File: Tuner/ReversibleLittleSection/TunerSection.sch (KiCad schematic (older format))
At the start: 113 parts, among them J1 Conn_01x03, J10 Conn_01x02, J11 Conn_02x05_Odd_Even, J12 Conn_01x01, J13 Conn_01x01, J14 Conn_01x01, J15 Conn_01x01, J2 Conn_01x03, J3 Conn_01x03, J4 Conn_01x03, J5 Conn_01x03, J6 Conn_01x03, J7 Conn_01x03, J8 Conn_01x02, J9 Conn_01x02, P10 Conn_01x01, P11 Conn_01x01, P12 Conn_01x01, P2 Conn_01x01, P3 Conn_01x01, P4 Conn_01x01, P5 Conn_01x01, P6 Conn_01x01, P7 Conn_01x01, P8 Conn_01x01, P9 Conn_01x01, U1 MCP23008, U2 ULN2803A

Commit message: JLCPCB Nov 1 2018
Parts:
- removed C36, C37: 10 nF, Capacitors_THT:C_Disc_D5.0mm_W2.5mm_P5.00mm, symbol C
- added J16, J17, J18, J19, J20, J21, J22: Conn_01x01, tuner:SOLDERJUMPER, symbol Conn_01x01
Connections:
- net RFGND: now also J16.1 (Pin_1)
- net at J9.2 (Pin_2), RLY9.2 (NC): now also J22.1 (Pin_1)
- net at J10.2 (Pin_2), RLY9.3 (NO): now also J17.1 (Pin_1)
- net at J15.1 (Pin_1): now also J18.1 (Pin_1), J19.1 (Pin_1)
- net at J12.1 (Pin_1): now also J20.1 (Pin_1), J21.1 (Pin_1)
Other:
- moved on the sheet: J15
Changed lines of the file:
@@
 RLY8
 $Comp
-L +5V #PWR13
+L +5V #PWR01
 U 1 1 5B1A0287
 P 3150 5750
-F 0 "#PWR13" H 3150 5600 50  0001 C CNN
+F 0 "#PWR01" H 3150 5600 50  0001 C CNN
 F 1 "+5V" H 3150 5890 50  0000 C CNN
 F 2 "" H 3150 5750 50  0001 C CNN
@@
 $EndComp
 $Comp
-L GND #PWR3
+L GND #PWR02
 U 1 1 5B1AA0F6
 P 900 4500
-F 0 "#PWR3" H 900 4250 50  0001 C CNN
+F 0 "#PWR02" H 900 4250 50  0001 C CNN
 F 1 "GND" H 900 4350 50  0000 C CNN
 F 2 "" H 900 4500 50  0001 C CNN
@@
 $EndComp
 $Comp
-L +5V #PWR2
+L +5V #PWR03
 U 1 1 5B1AABE9
 P 900 3750
-F 0 "#PWR2" H 900 3600 50  0001 C CNN
+F 0 "#PWR03" H 900 3600 50  0001 C CNN
 F 1 "+5V" H 900 3890 50  0000 C CNN
 F 2 "" H 900 3750 50  0001 C CNN
@@
 $EndComp
 $Comp
-L +5V #PWR9
+L +5V #PWR04
 U 1 1 5B1ABA5A
 P 2150 4450
-F 0 "#PWR9" H 2150 4300 50  0001 C CNN
+F 0 "#PWR04" H 2150 4300 50  0001 C CNN
 F 1 "+5V" H 2150 4590 50  0000 C CNN
 F 2 "" H 2150 4450 50  0001 C CNN
@@
 $EndComp
 $Comp
-L +5V #PWR11
+L +5V #PWR05
 U 1 1 5B1ABCDE
 P 2400 3950
-F 0 "#PWR11" H 2400 3800 50  0001 C CNN
+F 0 "#PWR05" H 2400 3800 50  0001 C CNN
 F 1 "+5V" H 2400 4090 50  0000 C CNN
 F 2 "" H 2400 3950 50  0001 C CNN
@@
 $EndComp
 $Comp
-L +5V #PWR17
+L +5V #PWR06
 U 1 1 5B1ABFC6
 P 8800 4600
-F 0 "#PWR17" H 8800 4450 50  0001 C CNN
+F 0 "#PWR06" H 8800 4450 50  0001 C CNN
 F 1 "+5V" H 8800 4740 50  0000 C CNN
 F 2 "" H 8800 4600 50  0001 C CNN
@@
 $EndComp
 $Comp
-L GND #PWR18
+L GND #PWR07
 U 1 1 5B1AC04C
 P 8800 5050
-F 0 "#PWR18" H 8800 4800 50  0001 C CNN
+F 0 "#PWR07" H 8800 4800 50  0001 C CNN
 F 1 "GND" H 8800 4900 50  0000 C CNN
 F 2 "" H 8800 5050 50  0001 C CNN
@@
 L Conn_01x01 J15
 U 1 1 5B19812D
-P 10950 950
-F 0 "J15" H 10950 1050 50  0000 C CNN
-F 1 "Conn_01x01" H 10950 850 50  0000 C CNN
-F 2 "Connectors:1pin" H 10950 950 50  0001 C CNN
-F 3 "" H 10950 950 50  0001 C CNN
-	1    10950 950
-	1    0    0    -1
-$EndComp
-$Comp
-L Conn_01x01 J12
-U 1 1 5B1981D8
-P 10950 1250
-F 0 "J12" H 10950 1350 50  0000 C CNN
-F 1 "Conn_01x01" H 10950 1150 50  0000 C CNN
-F 2 "Connectors:1pin" H 10950 1250 50  0001 C CNN
-F 3 "" H 10950 1250 50  0001 C CNN
-	1    10950 1250
+P 11100 750
+F 0 "J15" H 11100 850 50  0000 C CNN
+F 1 "Conn_01x01" H 11100 650 50  0000 C CNN
+F 2 "Connectors:1pin" H 11100 750 50  0001 C CNN
+F 3 "" H 11100 750 50  0001 C CNN
+	1    11100 750
 	1    0    0    -1
 $EndComp
@@
 $EndComp
 $Comp
-L +5V #PWR10
+L +5V #PWR08
 U 1 1 5B196BCE
 P 2250 3950
-F 0 "#PWR10" H 2250 3800 50  0001 C CNN
+F 0 "#PWR08" H 2250 3800 50  0001 C CNN
 F 1 "+5V" H 2250 4090 50  0000 C CNN
 F 2 "" H 2250 3950 50  0001 C CNN
@@
 $EndComp
 $Comp
-L GND #PWR15
+L GND #PWR09
 U 1 1 5B9A4AE1
 P 4850 6650
-F 0 "#PWR15" H 4850 6400 50  0001 C CNN
+F 0 "#PWR09" H 4850 6400 50  0001 C CNN
 F 1 "GND" H 4850 6500 50  0000 C CNN
 F 2 "" H 4850 6650 50  0001 C CNN
@@
 $EndComp
 $Comp
-L GND #PWR12
+L GND #PWR010
 U 1 1 5B9A6036
 P 3150 4200
-F 0 "#PWR12" H 3150 3950 50  0001 C CNN
+F 0 "#PWR010" H 3150 3950 50  0001 C CNN
 F 1 "GND" H 3150 4050 50  0000 C CNN
 F 2 "" H 3150 4200 50  0001 C CNN
@@
 $EndComp
 $Comp
-L GND #PWR14
+L GND #PWR011
 U 1 1 5B9ACA36
 P 3550 6100
-F 0 "#PWR14" H 3550 5850 50  0001 C CNN
+F 0 "#PWR011" H 3550 5850 50  0001 C CNN
 F 1 "GND" H 3550 5950 50  0000 C CNN
 F 2 "" H 3550 6100 50  0001 C CNN
@@
 $EndComp
 $Comp
-L GND #PWR19
+L GND #PWR012
 U 1 1 5B982525
 P 9850 2000
-F 0 "#PWR19" H 9850 1750 50  0001 C CNN
+F 0 "#PWR012" H 9850 1750 50  0001 C CNN
 F 1 "GND" H 9850 1850 50  0000 C CNN
 F 2 "" H 9850 2000 50  0001 C CNN
@@
 $EndComp
 $Comp
-L GND #PWR7
+L GND #PWR013
 U 1 1 5BA4D8F3
 P 1800 5850
-F 0 "#PWR7" H 1800 5600 50  0001 C CNN
+F 0 "#PWR013" H 1800 5600 50  0001 C CNN
 F 1 "GND" H 1800 5700 50  0000 C CNN
 F 2 "" H 1800 5850 50  0001 C CNN
@@
 $EndComp
 $Comp
-L +5V #PWR8
+L +5V #PWR014
 U 1 1 5BA4E273
 P 1850 5300
-F 0 "#PWR8" H 1850 5150 50  0001 C CNN
+F 0 "#PWR014" H 1850 5150 50  0001 C CNN
 F 1 "+5V" H 1850 5440 50  0000 C CNN
 F 2 "" H 1850 5300 50  0001 C CNN
@@
 $EndComp
 $Comp
-L +5V #PWR6
+L +5V #PWR015
 U 1 1 5BA4E663
 P 1200 5700
-F 0 "#PWR6" H 1200 5550 50  0001 C CNN
+F 0 "#PWR015" H 1200 5550 50  0001 C CNN
 F 1 "+5V" H 1200 5840 50  0000 C CNN
 F 2 "" H 1200 5700 50  0001 C CNN
@@
 $EndComp
 $Comp
-L GND #PWR1
+L GND #PWR016
 U 1 1 5BA4FB25
 P 750 5900
-F 0 "#PWR1" H 750 5650 50  0001 C CNN
+F 0 "#PWR016" H 750 5650 50  0001 C CNN
 F 1 "GND" H 750 5750 50  0000 C CNN
 F 2 "" H 750 5900 50  0001 C CNN
@@
 $EndComp
 $Comp
-L GND #PWR5
+L GND #PWR017
 U 1 1 5BA5005D
 P 1100 5300
-F 0 "#PWR5" H 1100 5050 50  0001 C CNN
+F 0 "#PWR017" H 1100 5050 50  0001 C CNN
 F 1 "GND" H 1100 5150 50  0000 C CNN
 F 2 "" H 1100 5300 50  0001 C CNN
@@
 EXTPWR
 $Comp
-L +5V #PWR4
+L +5V #PWR018
 U 1 1 5BAE4DBC
 P 1000 4850
-F 0 "#PWR4" H 1000 4700 50  0001 C CNN
+F 0 "#PWR018" H 1000 4700 50  0001 C CNN
 F 1 "+5V" H 1000 4990 50  0000 C CNN
 F 2 "" H 1000 4850 50  0001 C CNN
@@
 	700  4850 1000 4850
 $Comp
-L GND #PWR16
+L GND #PWR019
 U 1 1 5BAEE216
 P 5050 7250
-F 0 "#PWR16" H 5050 7000 50  0001 C CNN
+F 0 "#PWR019" H 5050 7000 50  0001 C CNN
 F 1 "GND" H 5050 7100 50  0000 C CNN
 F 2 "" H 5050 7250 50  0001 C CNN
@@
 	10400 2550 10400 2250
 Connection ~ 10400 2250
-Text GLabel 10100 1250 0    60   Input ~ 0
+Text GLabel 9550 750  0    60   Input ~ 0
 RFGND
 $Comp
-L C C37
-U 1 1 5BCC2C84
-P 10500 1250
-F 0 "C37" H 10525 1350 50  0000 L CNN
-F 1 "10 nF" H 10525 1150 50  0000 L CNN
-F 2 "Capacitors_THT:C_Disc_D5.0mm_W2.5mm_P5.00mm" H 10538 1100 50  0001 C CNN
-F 3 "" H 10500 1250 50  0001 C CNN
-	1    10500 1250
-	0    1    1    0
-$EndComp
-Wire Wire Line
-	10650 1250 10750 1250
-Wire Wire Line
-	10100 1250 10350 1250
-$Comp
-L C C36
-U 1 1 5BCFB23A
-P 10500 950
-F 0 "C36" H 10525 1050 50  0000 L CNN
-F 1 "10 nF" H 10525 850 50  0000 L CNN
-F 2 "Capacitors_THT:C_Disc_D5.0mm_W2.5mm_P5.00mm" H 10538 800 50  0001 C CNN
-F 3 "" H 10500 950 50  0001 C CNN
-	1    10500 950
-	0    1    1    0
-$EndComp
-Text GLabel 10100 950  0    60   Input ~ 0
-RFGND
-Wire Wire Line
-	10100 950  10350 950
-Wire Wire Line
-	10650 950  10750 950
+L Conn_01x01 J16
+U 1 1 5BD88254
+P 9850 750
+F 0 "J16" H 9850 850 50  0000 C CNN
+F 1 "Conn_01x01" H 9850 650 50  0000 C CNN
+F 2 "tuner:SOLDERJUMPER" H 9850 750 50  0001 C CNN
+F 3 "" H 9850 750 50  0001 C CNN
+	1    9850 750
+	1    0    0    -1
+$EndComp
+Wire Wire Line
+	9650 750  9550 750
+$Comp
+L Conn_01x01 J18
+U 1 1 5BD8893E
+P 10650 700
+F 0 "J18" H 10650 800 50  0000 C CNN
+F 1 "Conn_01x01" H 10650 600 50  0000 C CNN
+F 2 "tuner:SOLDERJUMPER" H 10650 700 50  0001 C CNN
+F 3 "" H 10650 700 50  0001 C CNN
+	1    10650 700
+	-1   0    0    1
+$EndComp
+$Comp
+L Conn_01x01 J19
+U 1 1 5BD88AB6
+P 10650 800
+F 0 "J19" H 10650 900 50  0000 C CNN
+F 1 "Conn_01x01" H 10650 700 50  0000 C CNN
+F 2 "tuner:SOLDERJUMPER" H 10650 800 50  0001 C CNN
+F 3 "" H 10650 800 50  0001 C CNN
+	1    10650 800
+	-1   0    0    1
+$EndComp
+Wire Wire Line
+	10850 700  10850 800
+Wire Wire Line
+	10850 750  10900 750
+Connection ~ 10850 750
+$Comp
+L Conn_01x01 J22
+U 1 1 5BD890B9
+P 9600 3750
+F 0 "J22" H 9600 3850 50  0000 C CNN
+F 1 "Conn_01x01" H 9600 3650 50  0000 C CNN
+F 2 "tuner:SOLDERJUMPER" H 9600 3750 50  0001 C CNN
+F 3 "" H 9600 3750 50  0001 C CNN
+	1    9600 3750
+	-1   0    0    1
+$EndComp
+$Comp
+L Conn_01x01 J20
+U 1 1 5BD8922D
+P 10650 950
+F 0 "J20" H 10650 1050 50  0000 C CNN
+F 1 "Conn_01x01" H 10650 850 50  0000 C CNN
+F 2 "tuner:SOLDERJUMPER" H 10650 950 50  0001 C CNN
+F 3 "" H 10650 950 50  0001 C CNN
+	1    10650 950
+	-1   0    0    1
+$EndComp
+$Comp
+L Conn_01x01 J21
+U 1 1 5BD8939E
+P 10650 1050
+F 0 "J21" H 10650 1150 50  0000 C CNN
+F 1 "Conn_01x01" H 10650 950 50  0000 C CNN
+F 2 "tuner:SOLDERJUMPER" H 10650 1050 50  0001 C CNN
+F 3 "" H 10650 1050 50  0001 C CNN
+	1    10650 1050
+	-1   0    0    1
+$EndComp
+Wire Wire Line
+	10850 950  10850 1050
+Wire Wire Line
+	10850 1000 10900 1000
+Connection ~ 10850 1000
+$Comp
+L Conn_01x01 J17
+U 1 1 5BD89B92
+P 10500 4000
+F 0 "J17" H 10500 4100 50  0000 C CNN
+F 1 "Conn_01x01" H 10500 3900 50  0000 C CNN
+F 2 "tuner:SOLDERJUMPER" H 10500 4000 50  0001 C CNN
+F 3 "" H 10500 4000 50  0001 C CNN
+	1    10500 4000
+	1    0    0    -1
+$EndComp
+Wire Wire Line
+	10300 4000 10150 4000
+Connection ~ 10150 4000
+$Comp
+L Conn_01x01 J12
+U 1 1 5BD8A2D9
+P 11100 1000
+F 0 "J12" H 11100 1100 50  0000 C CNN
+F 1 "Conn_01x01" H 11100 900 50  0000 C CNN
+F 2 "Connectors:1pin" H 11100 1000 50  0001 C CNN
+F 3 "" H 11100 1000 50  0001 C CNN
+	1    11100 1000
+	1    0    0    -1
+$EndComp
+Wire Wire Line
+	9800 3750 9900 3750
+Connection ~ 9900 3750
 $EndSCHEMATC

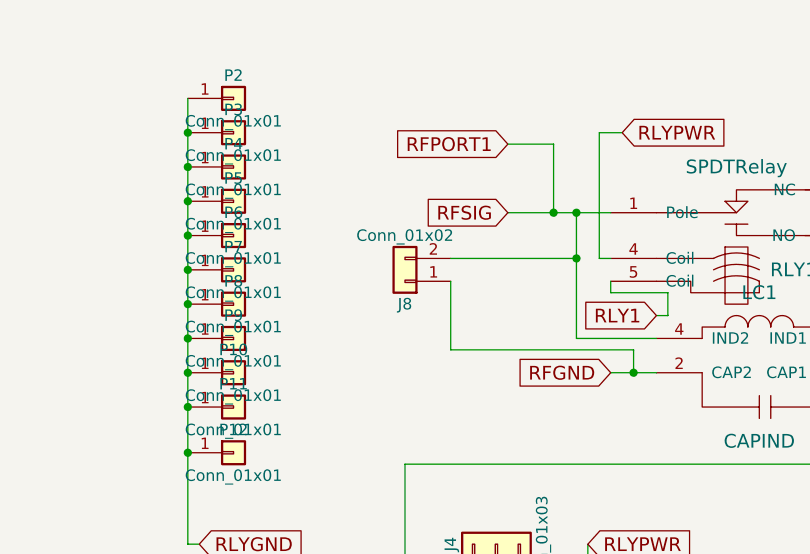
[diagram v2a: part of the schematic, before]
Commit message: Modified connectors on Reversible boards
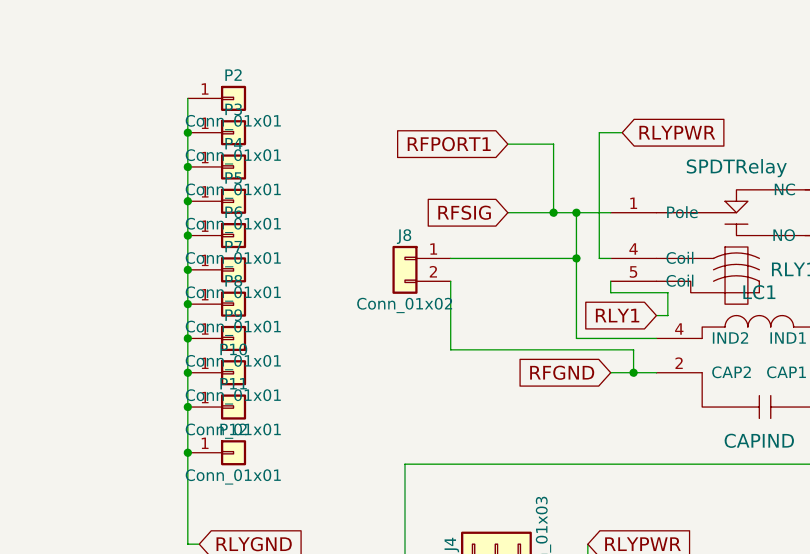
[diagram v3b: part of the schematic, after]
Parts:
- J10, J8, J9: footprint Connectors_Terminal_Blocks:TerminalBlock_bornier-2_P5.08mm -> tuner:bnc_90_1-1337543-0_pad_combo
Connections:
- net RFGND: now also J8.2 (Pin_2); no longer J8.1 (Pin_1)
- net RFPORT1: now also J8.1 (Pin_1); no longer J8.2 (Pin_2)
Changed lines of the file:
@@
 L Conn_01x02 J8
 U 1 1 5B18E79B
-P 2150 1700
-F 0 "J8" H 2150 1800 50  0000 C CNN
-F 1 "Conn_01x02" H 2150 1500 50  0000 C CNN
-F 2 "Connectors_Terminal_Blocks:TerminalBlock_bornier-2_P5.08mm" H 2150 1700 50  0001 C CNN
-F 3 "" H 2150 1700 50  0001 C CNN
-	1    2150 1700
-	-1   0    0    1
+P 2150 1600
+F 0 "J8" H 2150 1700 50  0000 C CNN
+F 1 "Conn_01x02" H 2150 1400 50  0000 C CNN
+F 2 "tuner:bnc_90_1-1337543-0_pad_combo" H 2150 1600 50  0001 C CNN
+F 3 "" H 2150 1600 50  0001 C CNN
+	1    2150 1600
+	-1   0    0    -1
 $EndComp
 $Comp
@@
 F 0 "J10" H 10350 3700 50  0000 C CNN
 F 1 "Conn_01x02" H 10350 3400 50  0000 C CNN
-F 2 "Connectors_Terminal_Blocks:TerminalBlock_bornier-2_P5.08mm" H 10350 3600 50  0001 C CNN
+F 2 "tuner:bnc_90_1-1337543-0_pad_combo" H 10350 3600 50  0001 C CNN
 F 3 "" H 10350 3600 50  0001 C CNN
 	1    10350 3600
@@
 F 0 "J9" H 10350 3200 50  0000 C CNN
 F 1 "Conn_01x02" H 10350 2900 50  0000 C CNN
-F 2 "Connectors_Terminal_Blocks:TerminalBlock_bornier-2_P5.08mm" H 10350 3100 50  0001 C CNN
+F 2 "tuner:bnc_90_1-1337543-0_pad_combo" H 10350 3100 50  0001 C CNN
 F 3 "" H 10350 3100 50  0001 C CNN
 	1    10350 3100

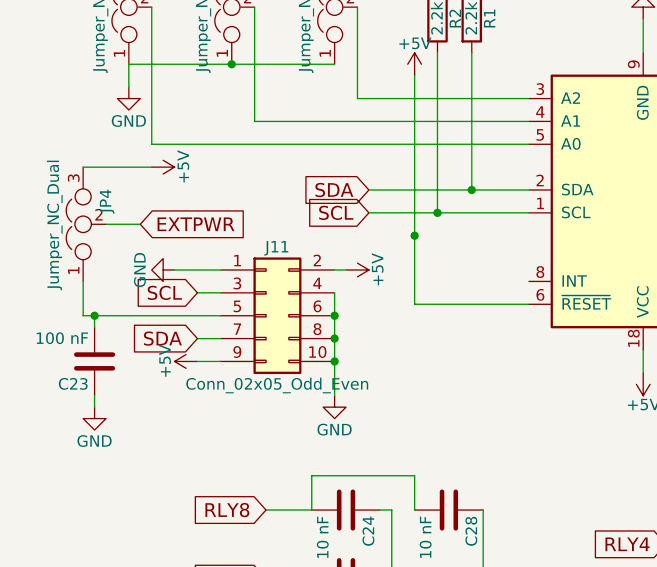
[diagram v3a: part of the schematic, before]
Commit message: Changed I2C cable pinoutgit add Tunergit add Tuner Also added ICOM rig support
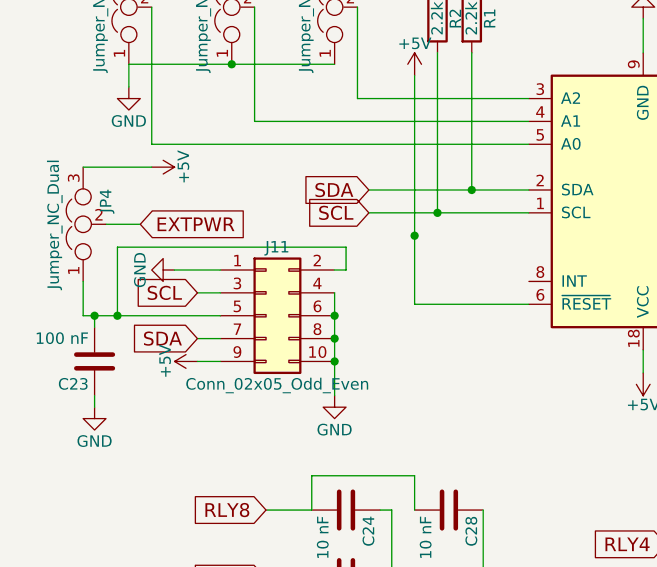
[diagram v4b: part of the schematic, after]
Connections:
- net +5V: no longer J11.2 (Pin_2)
- net at C23.2, J11.5 (Pin_5), JP4.1: now also J11.2 (Pin_2)
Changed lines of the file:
@@
-$EndComp
-$Comp
-L +5V #PWR8
-U 1 1 5BA4E273
-P 1850 5300
-F 0 "#PWR8" H 1850 5150 50  0001 C CNN
-F 1 "+5V" H 1850 5440 50  0000 C CNN
-F 2 "" H 1850 5300 50  0001 C CNN
-F 3 "" H 1850 5300 50  0001 C CNN
-	1    1850 5300
-	0    1    1    0
 $EndComp
 $Comp
@@
 	9800 3750 9900 3750
 Connection ~ 9900 3750
+Wire Wire Line
+	850  5500 850  5200
+Wire Wire Line
+	850  5200 1850 5200
+Wire Wire Line
+	1850 5200 1850 5300
+Connection ~ 850  5500
 $EndSCHEMATC

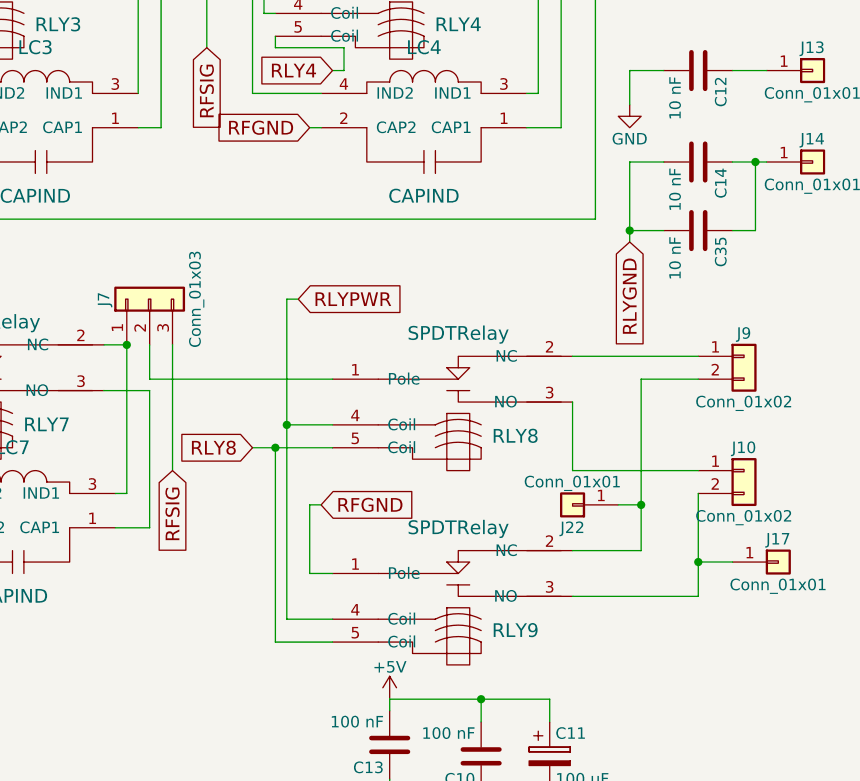
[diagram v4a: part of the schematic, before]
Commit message: Added nonswitched output to ReversibleSections
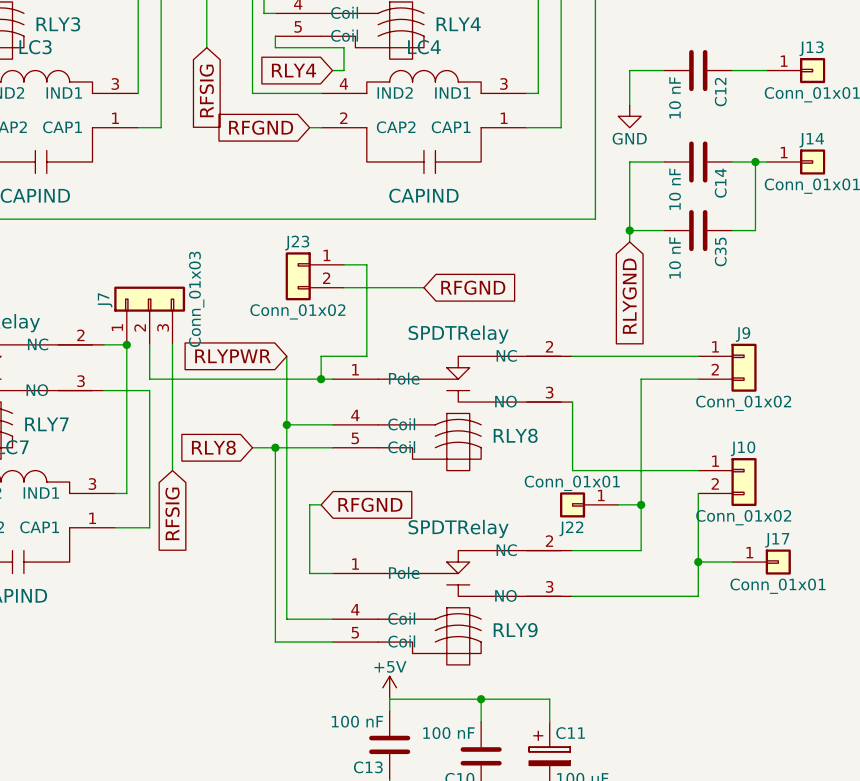
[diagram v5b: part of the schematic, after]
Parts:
- added J23: Conn_01x02, tuner:bnc_90_1-1337543-0_pad_combo, symbol Conn_01x02
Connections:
- net RFGND: now also J23.2 (Pin_2)
- net at J7.2 (Pin_2), RLY8.1 (Pole): now also J23.1 (Pin_1)
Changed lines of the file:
@@
 RLY8
 $Comp
-L +5V #PWR13
+L +5V #PWR12
 U 1 1 5B1A0287
 P 3150 5750
-F 0 "#PWR13" H 3150 5600 50  0001 C CNN
+F 0 "#PWR12" H 3150 5600 50  0001 C CNN
 F 1 "+5V" H 3150 5890 50  0000 C CNN
 F 2 "" H 3150 5750 50  0001 C CNN
@@
 $EndComp
 $Comp
-L +5V #PWR9
+L +5V #PWR8
 U 1 1 5B1ABA5A
 P 2150 4450
-F 0 "#PWR9" H 2150 4300 50  0001 C CNN
+F 0 "#PWR8" H 2150 4300 50  0001 C CNN
 F 1 "+5V" H 2150 4590 50  0000 C CNN
 F 2 "" H 2150 4450 50  0001 C CNN
@@
 $EndComp
 $Comp
-L +5V #PWR11
+L +5V #PWR10
 U 1 1 5B1ABCDE
 P 2400 3950
-F 0 "#PWR11" H 2400 3800 50  0001 C CNN
+F 0 "#PWR10" H 2400 3800 50  0001 C CNN
 F 1 "+5V" H 2400 4090 50  0000 C CNN
 F 2 "" H 2400 3950 50  0001 C CNN
@@
 $EndComp
 $Comp
-L +5V #PWR10
+L +5V #PWR9
 U 1 1 5B196BCE
 P 2250 3950
-F 0 "#PWR10" H 2250 3800 50  0001 C CNN
+F 0 "#PWR9" H 2250 3800 50  0001 C CNN
 F 1 "+5V" H 2250 4090 50  0000 C CNN
 F 2 "" H 2250 3950 50  0001 C CNN
@@
 $EndComp
 $Comp
-L GND #PWR15
+L GND #PWR14
 U 1 1 5B9A4AE1
 P 4850 6650
-F 0 "#PWR15" H 4850 6400 50  0001 C CNN
+F 0 "#PWR14" H 4850 6400 50  0001 C CNN
 F 1 "GND" H 4850 6500 50  0000 C CNN
 F 2 "" H 4850 6650 50  0001 C CNN
@@
 $EndComp
 $Comp
-L GND #PWR12
+L GND #PWR11
 U 1 1 5B9A6036
 P 3150 4200
-F 0 "#PWR12" H 3150 3950 50  0001 C CNN
+F 0 "#PWR11" H 3150 3950 50  0001 C CNN
 F 1 "GND" H 3150 4050 50  0000 C CNN
 F 2 "" H 3150 4200 50  0001 C CNN
@@
 $EndComp
 $Comp
-L GND #PWR14
+L GND #PWR13
 U 1 1 5B9ACA36
 P 3550 6100
-F 0 "#PWR14" H 3550 5850 50  0001 C CNN
+F 0 "#PWR13" H 3550 5850 50  0001 C CNN
 F 1 "GND" H 3550 5950 50  0000 C CNN
 F 2 "" H 3550 6100 50  0001 C CNN
@@
 Text GLabel 6550 2800 2    60   Input ~ 0
 RLYPWR
-Text GLabel 8400 2850 2    60   Input ~ 0
+Text GLabel 8350 3100 0    60   Input ~ 0
 RLYPWR
 Text GLabel 8300 1050 2    60   Input ~ 0
@@
 $EndComp
 $Comp
-L GND #PWR16
+L GND #PWR15
 U 1 1 5BAEE216
 P 5050 7250
-F 0 "#PWR16" H 5050 7000 50  0001 C CNN
+F 0 "#PWR15" H 5050 7000 50  0001 C CNN
 F 1 "GND" H 5050 7100 50  0000 C CNN
 F 2 "" H 5050 7250 50  0001 C CNN
@@
 Connection ~ 7650 3050
 Wire Wire Line
-	10150 4150 10150 3700
-Wire Wire Line
-	9600 4150 10150 4150
+	10150 3700 10150 4150
+Wire Wire Line
+	10150 4150 9600 4150
 Wire Wire Line
 	9900 3200 10150 3200
 Wire Wire Line
-	9900 3950 9900 3200
+	9900 3200 9900 3950
 Wire Wire Line
 	9600 3600 10150 3600
@@
 	9600 3300 9600 3600
 Wire Wire Line
-	9600 3950 9900 3950
+	9900 3950 9600 3950
 Wire Wire Line
 	9600 3100 10150 3100
@@
 	8350 3400 8550 3400
 Wire Wire Line
-	8350 2850 8350 4250
+	8350 3100 8350 4250
 Connection ~ 9200 5000
 Connection ~ 9200 4600
@@
 	6450 2800 6550 2800
 Wire Wire Line
-	8400 2850 8350 2850
-Wire Wire Line
 	8300 1050 8250 1050
 Wire Wire Line
@@
 	10300 2250 10450 2250
 Wire Wire Line
-	9850 2600 9850 2250
+	9850 2250 9850 2600
 Wire Wire Line
 	9850 2250 10000 2250
@@
 	1850 5200 1850 5300
 Connection ~ 850  5500
+$Comp
+L Conn_01x02 J23
+U 1 1 5C9BB02B
+P 8400 2700
+F 0 "J23" H 8400 2800 50  0000 C CNN
+F 1 "Conn_01x02" H 8400 2500 50  0000 C CNN
+F 2 "tuner:bnc_90_1-1337543-0_pad_combo" H 8400 2700 50  0001 C CNN
+F 3 "" H 8400 2700 50  0001 C CNN
+	1    8400 2700
+	-1   0    0    -1
+$EndComp
+Wire Wire Line
+	8600 2700 8700 2700
+Wire Wire Line
+	8700 2700 8700 3100
+Wire Wire Line
+	8700 3100 8500 3100
+Wire Wire Line
+	8500 3100 8500 3200
+Connection ~ 8500 3200
+Text GLabel 8950 2800 2    60   Input ~ 0
+RFGND
+Wire Wire Line
+	8950 2800 8600 2800
 $EndSCHEMATC
